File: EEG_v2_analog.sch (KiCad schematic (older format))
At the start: 35 parts, among them J1 BIAS, J10 IN5P, J11 IN5N, J12 IN6P, J13 IN6N, J14 IN7P, J15 IN7N, J16 IN8P, J17 IN8N, J18 SRB1, J19 SRB2, J2 IN1P, J3 IN1N, J4 IN2P, J5 IN2N, J6 IN3P, J7 IN3N, J8 IN4P, J9 IN4N, U1 ADS1299IPAGR

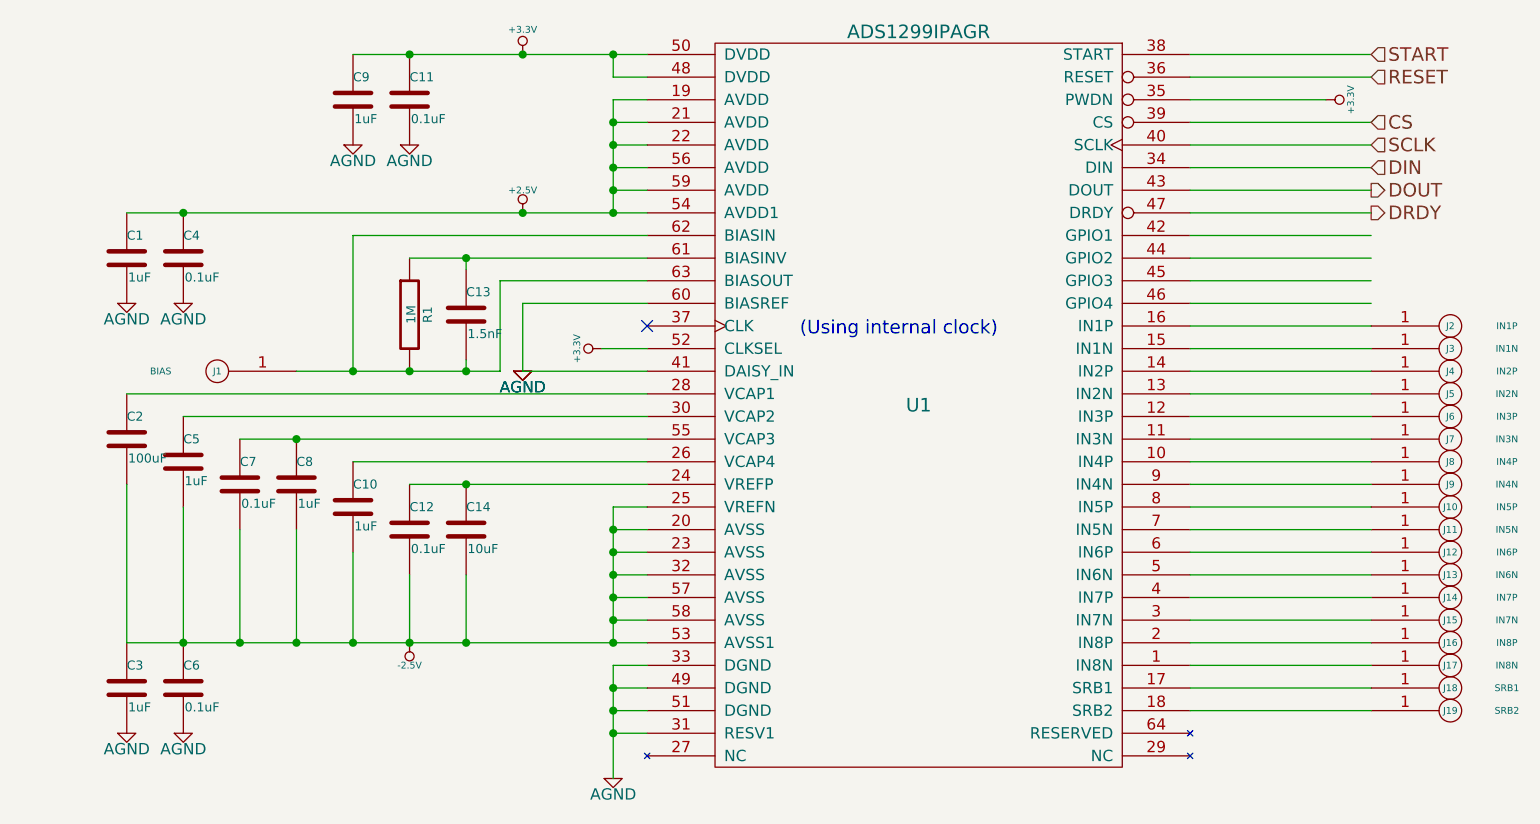
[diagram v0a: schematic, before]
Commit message: Added footprints to ADS caps, shorted unused GPIO to gnd
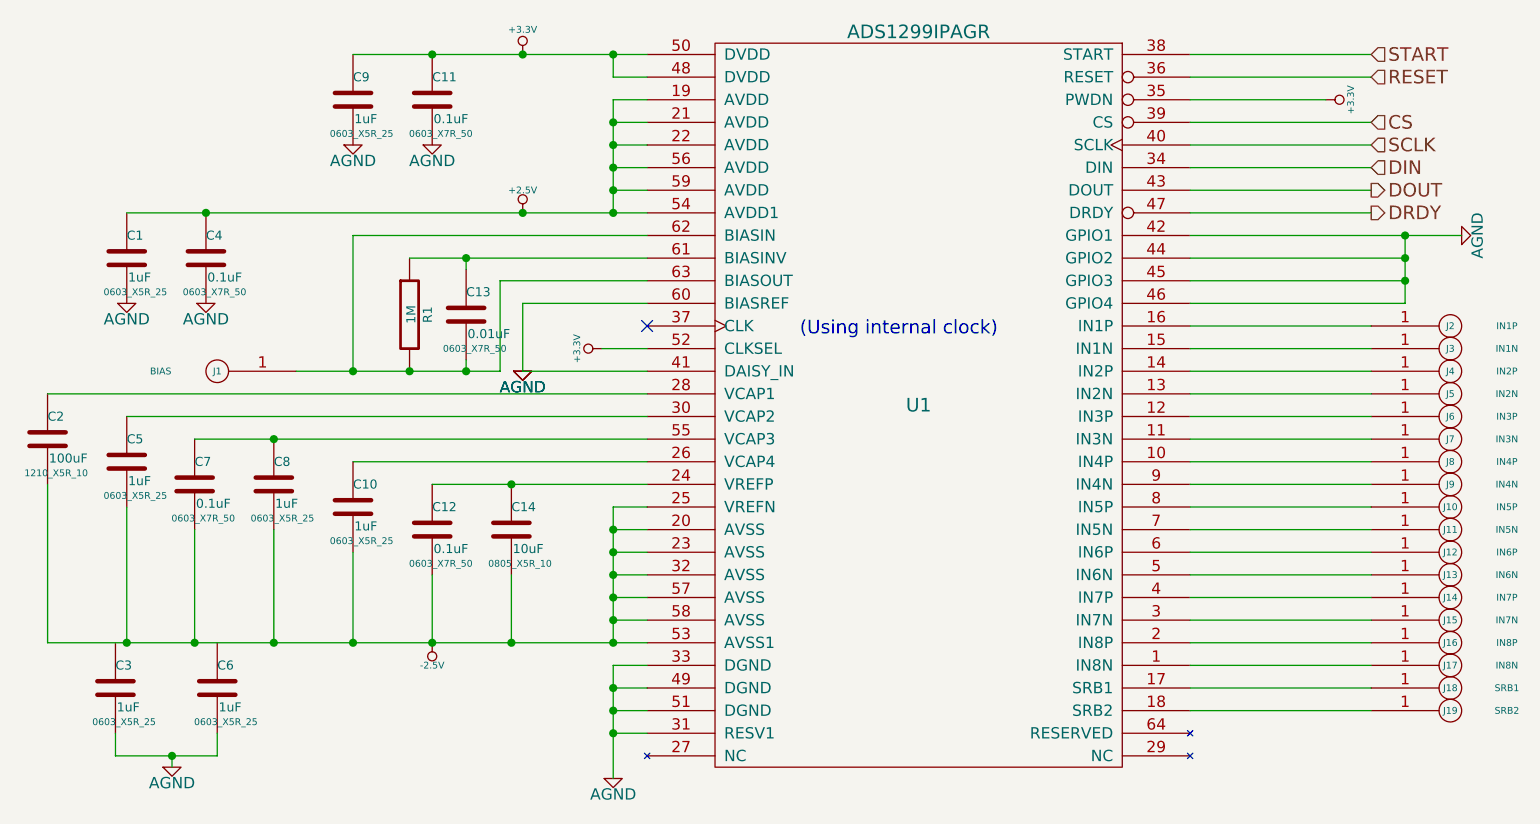
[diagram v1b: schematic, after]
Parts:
- C1, C10, C3, C5, C8, C9: footprint ~ -> 0603_X5R_25
- C11, C12, C4, C7: footprint ~ -> 0603_X7R_50
- C13: value 1.5nF -> 0.01uF; footprint ~ -> 0603_X7R_50
- C14: footprint ~ -> 0805_X5R_10
- C2: footprint ~ -> 1210_X5R_10
- C6: value 0.1uF -> 1uF; footprint ~ -> 0603_X5R_25
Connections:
- wire segments 77 -> 82
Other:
- moved on the sheet: C11, C12, C14, C2, C3, C4, C5, C6, C7, C8

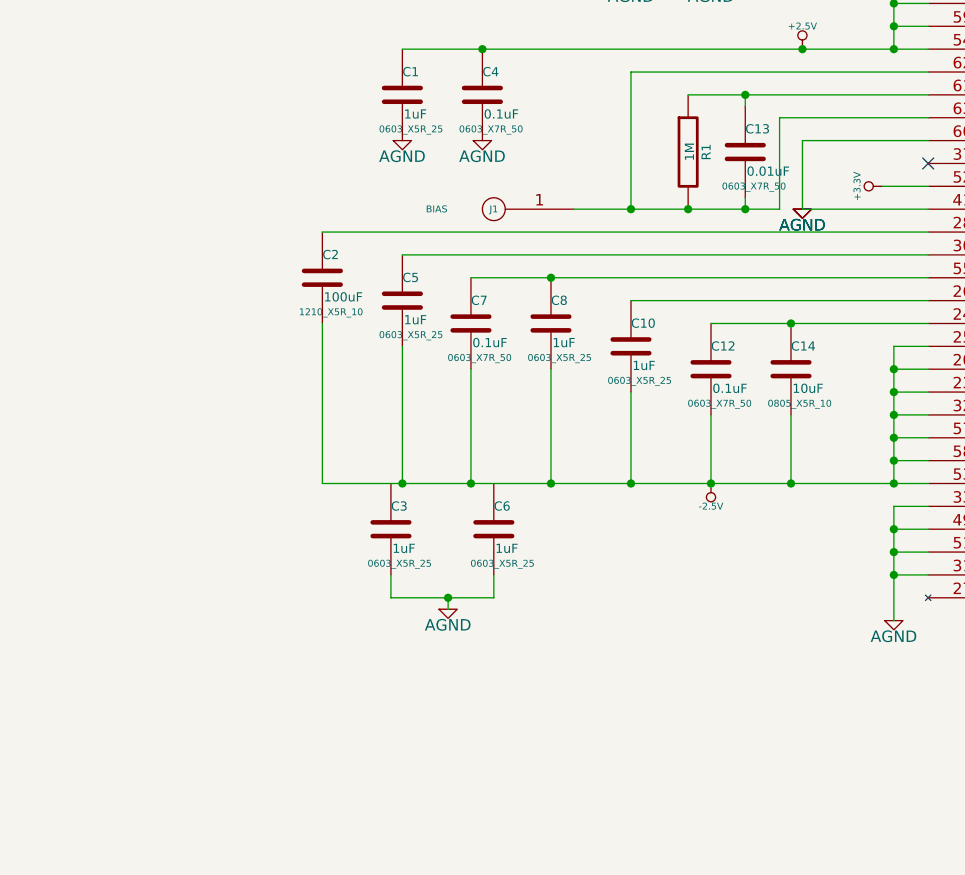
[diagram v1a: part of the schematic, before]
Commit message: Add decoupling caps btwn AVDD and AVSS
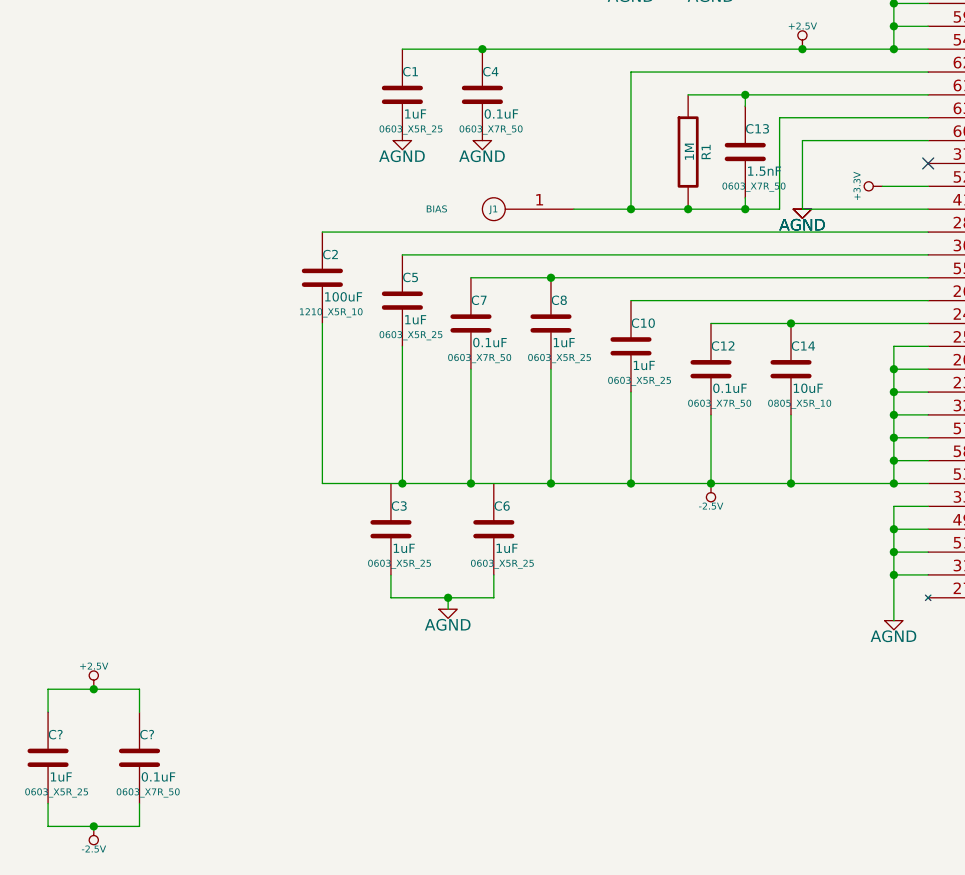
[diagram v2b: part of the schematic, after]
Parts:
- added C?: 0.1uF, 0603_X7R_50, symbol C
- added C?: 1uF, 0603_X5R_25, symbol C
- C13: value 0.01uF -> 1.5nF
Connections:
- net +2.5V: now also C?.1, C?.1
- net -2.5V: now also C?.2, C?.2
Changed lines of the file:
@@
 P 4500 3650
 F 0 "C13" H 4500 3750 40  0000 L CNN
-F 1 "0.01uF" H 4506 3565 40  0000 L CNN
+F 1 "1.5nF" H 4506 3565 40  0000 L CNN
 F 2 "0603_X7R_50" H 4538 3500 30  0000 C CNN
 F 3 "~" H 4500 3650 60  0000 C CNN
@@
 Connection ~ 8650 3400
 Connection ~ 8650 3500
+$Comp
+L C C?
+U 1 1 54C4F289
+P 1850 6300
+F 0 "C?" H 1850 6400 40  0000 L CNN
+F 1 "0.1uF" H 1856 6215 40  0000 L CNN
+F 2 "0603_X7R_50" H 1888 6150 30  0000 C CNN
+F 3 "~" H 1850 6300 60  0000 C CNN
+	1    1850 6300
+	1    0    0    -1
+$EndComp
+$Comp
+L C C?
+U 1 1 54C4F28F
+P 1450 6300
+F 0 "C?" H 1450 6400 40  0000 L CNN
+F 1 "1uF" H 1456 6215 40  0000 L CNN
+F 2 "0603_X5R_25" H 1488 6150 30  0000 C CNN
+F 3 "~" H 1450 6300 60  0000 C CNN
+	1    1450 6300
+	1    0    0    -1
+$EndComp
+$Comp
+L -2.5V #PWR?
+U 1 1 54C4F2A1
+P 1650 6600
+F 0 "#PWR?" H 1650 6550 20  0001 C CNN
+F 1 "-2.5V" H 1650 6700 30  0000 C CNN
+F 2 "" H 1650 6600 60  0000 C CNN
+F 3 "" H 1650 6600 60  0000 C CNN
+	1    1650 6600
+	-1   0    0    1
+$EndComp
+$Comp
+L +2.5V #PWR?
+U 1 1 54C4F2B1
+P 1650 6000
+F 0 "#PWR?" H 1650 5950 20  0001 C CNN
+F 1 "+2.5V" H 1650 6100 30  0000 C CNN
+F 2 "" H 1650 6000 60  0000 C CNN
+F 3 "" H 1650 6000 60  0000 C CNN
+	1    1650 6000
+	1    0    0    -1
+$EndComp
+Wire Wire Line
+	1450 6100 1450 6000
+Wire Wire Line
+	1450 6000 1850 6000
+Wire Wire Line
+	1850 6000 1850 6100
+Connection ~ 1650 6000
+Wire Wire Line
+	1850 6600 1850 6500
+Wire Wire Line
+	1450 6600 1850 6600
+Wire Wire Line
+	1450 6500 1450 6600
+Connection ~ 1650 6600
 $EndSCHEMATC
